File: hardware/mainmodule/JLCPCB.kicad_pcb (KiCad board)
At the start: 2 copper layers, 83.8 x 61 mm, 73 parts, among them J1 USB+, J10 Conn_01x04, J2 To LED_MOD_0, J3 To EXT_MOD_1, J4 V24_IN, J5 Temp, J6 Presence, J7 Neo, J8 AUX, J9 Conn_01x04, Q1 Si3456DDV, Q2 Si3456DDV, Q3 Si3456DDV, Q4 Si3456DDV, Q5 Si3456DDV, Q6 Si3456DDV, SW1 SW_Push, SW2 SW_Push, U1 ESP32-C6-WROOM-1, U3 74HCT244, U4 DS18B20, U5 MC34063AD, U6 DT1042-04SO1

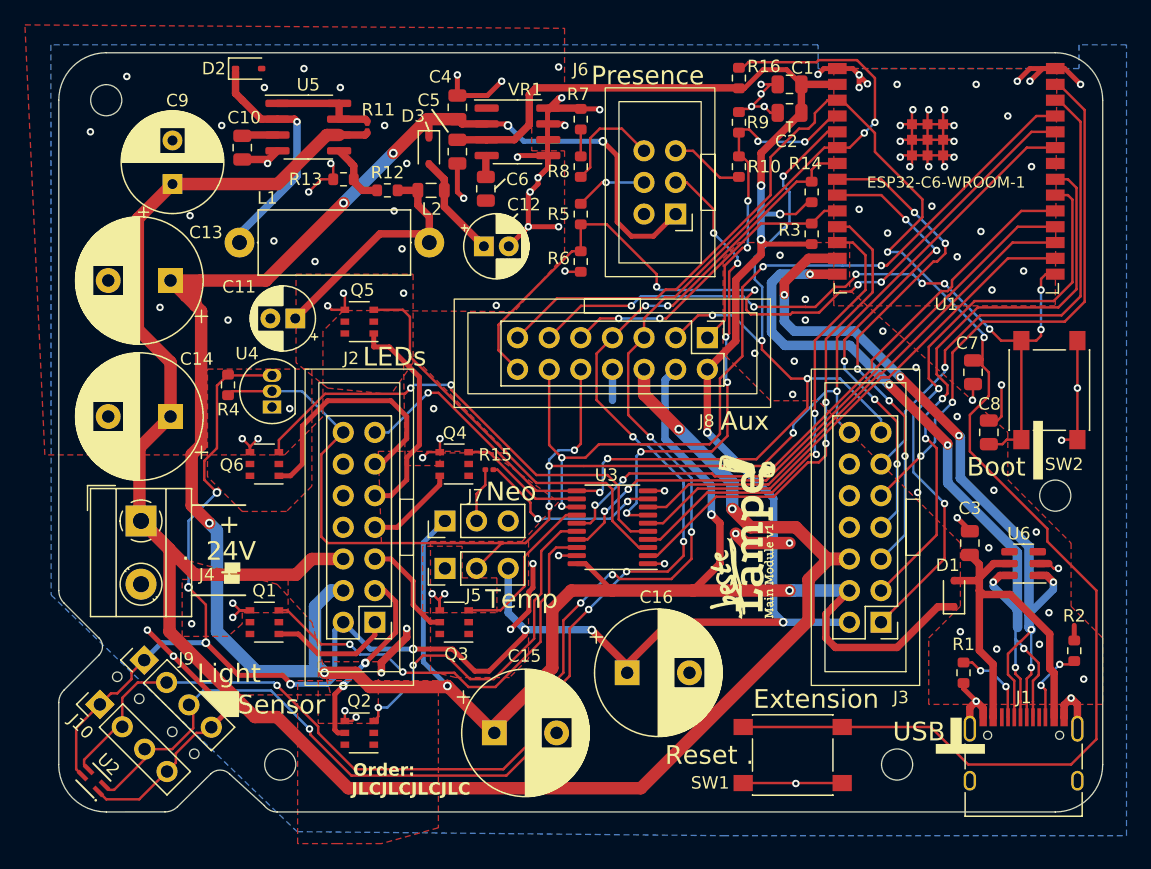
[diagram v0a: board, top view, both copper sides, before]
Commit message: Larger resistor footprints, includes some other property updates.
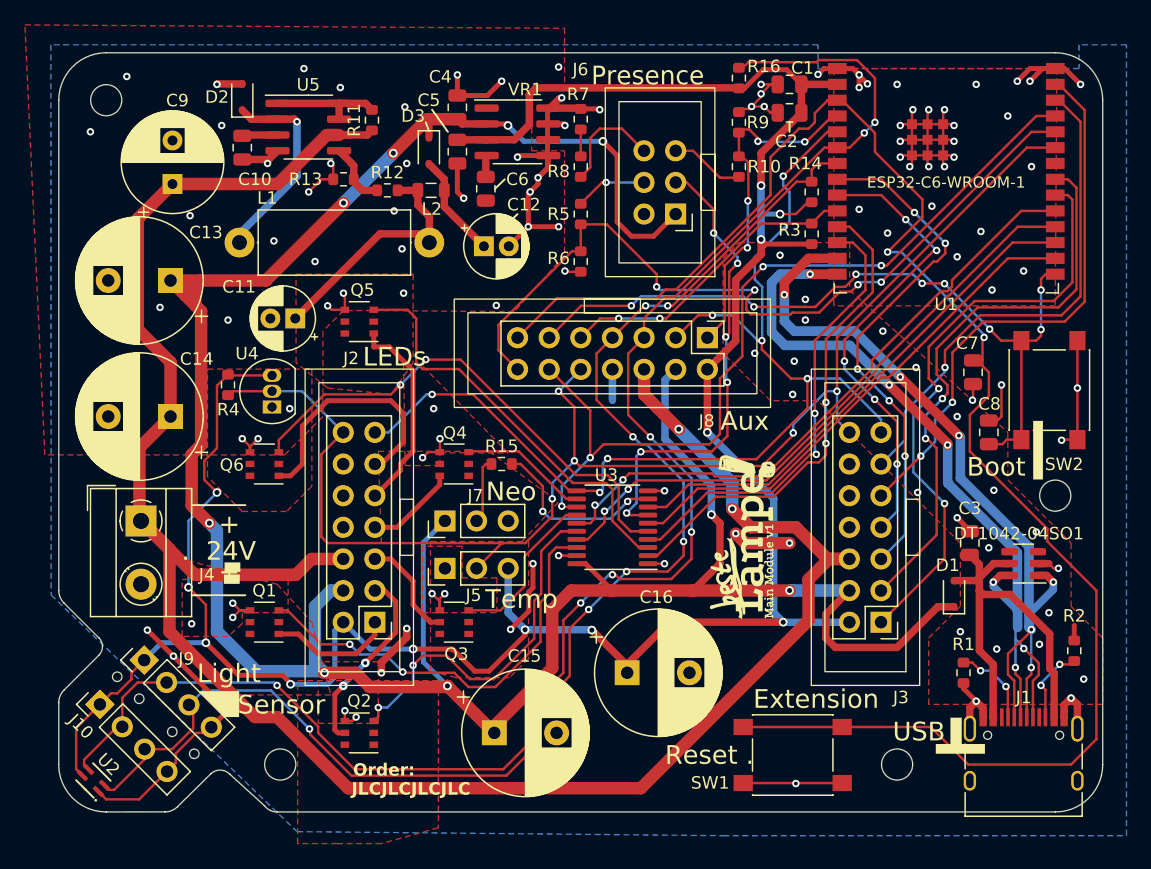
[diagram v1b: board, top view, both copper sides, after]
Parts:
- DT1042-04SO1: renamed from U6; value DT1042-04SO1 -> ~
- R11, R15: footprint Resistor_SMD:R_0201_0603Metric -> Resistor_SMD:R_0603_1608Metric
- U2: renamed from ?; value (none) -> ~
- moved D2 2.34 mm to (79.5, 51.8), turned to 90 degrees
- moved R15 1.09 mm to (100.3, 81.3)
- moved R11 0.68 mm to (89.9, 53.7)
- renumbered H1 to H3
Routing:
- net Net-(D2-K): track 18.8 -> 15.7 mm
- net GND: track 193.4 -> 195.4 mm
- net /TEMP: track 114.8 -> 113.3 mm
- net /DR0.6: track 39.1 -> 40.6 mm
- net /L0.5: track 17.5 -> 16.3 mm
- net Net-(J7-Pin_2): track 4.41 -> 5.33 mm
- net /DR_NEO: track 15.2 -> 14.6 mm
- net Net-(U5-DC): track 8.55 -> 9.07 mm

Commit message: Add two missing EN lines.
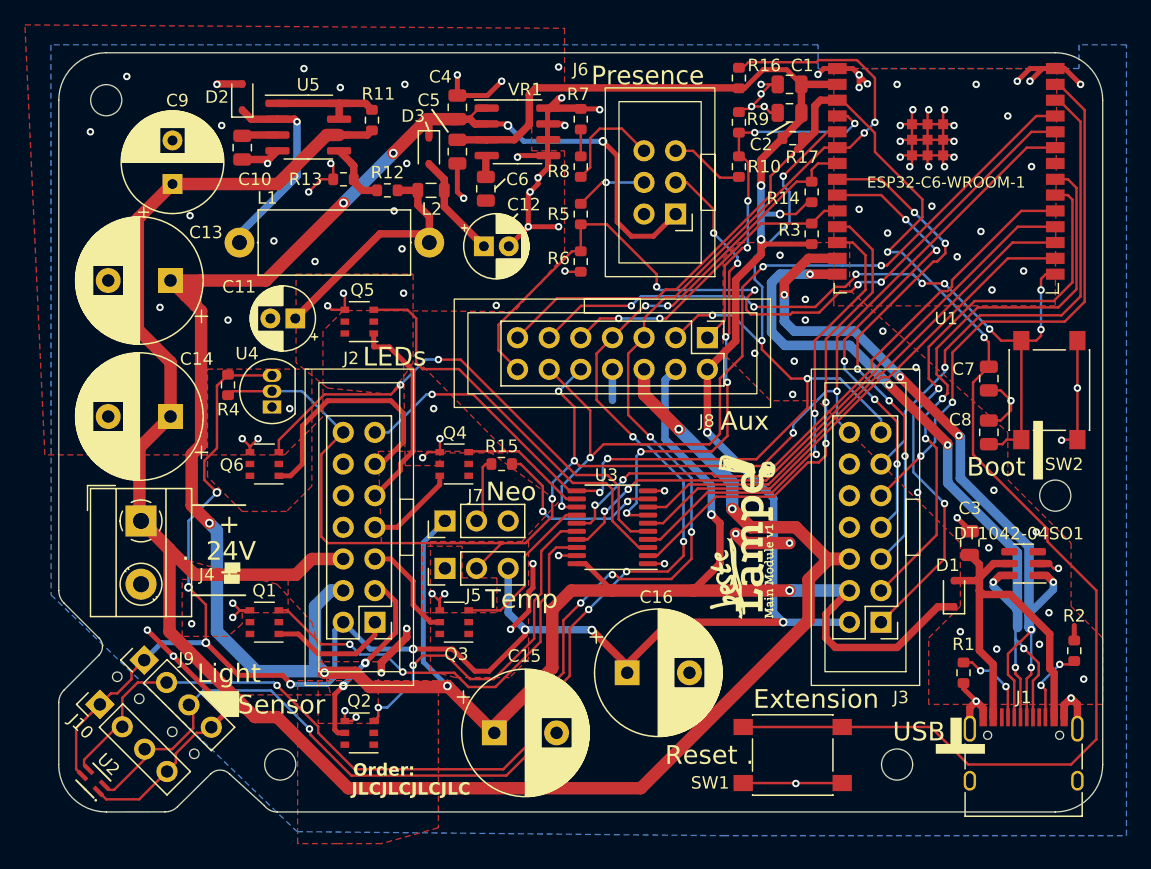
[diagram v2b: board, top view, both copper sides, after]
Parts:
- added R17: 10K, Resistor_SMD:R_0603_1608Metric, F.Cu at (123.7, 55.1)
- moved C7 1.37 mm to (139.4, 74.4)
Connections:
- VR1 pad 1: unconnected-(VR1-EN-Pad1) -> +5V
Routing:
- net +5V: track 215.5 -> 218.6 mm
- net /PRES_A_3V3: track 28.0 -> 30.3 mm
- net GND: vias 120 -> 118

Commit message: Add missing light sensor.
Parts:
- U2: value ~ -> VEML6040A3OG
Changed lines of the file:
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@@
   (footprint "footprints:OPLGA4" (layer "F.Cu")
     (at 67.558883 106.687909 135)
+    (property "LCSC" "C78465")
     (property "Sheetfile" "JLCPCB.kicad_sch")
     (property "Sheetname" "")
@@
         (effects (font (size 0.2 0.2) (thickness 0.05)))
     )
-    (fp_text value "~" (at 0 0.95 135) (layer "F.SilkS") hide
+    (fp_text value "VEML6040A3OG" (at 0 0.95 135) (layer "F.SilkS") hide
         (effects (font (size 0.2 0.2) (thickness 0.05)))
     )

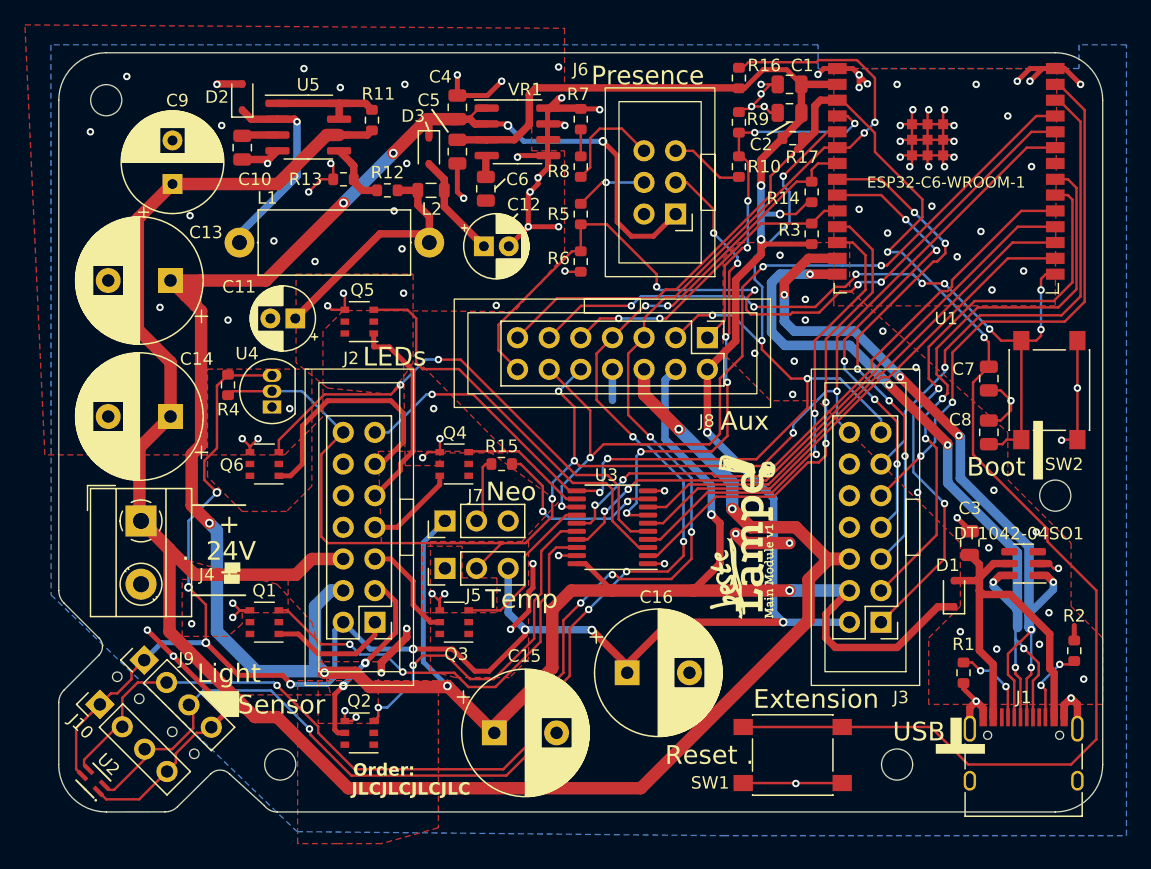
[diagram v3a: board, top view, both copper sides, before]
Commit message: Bigger mounting holes (for M3 screws) and less disconnected ground planes.
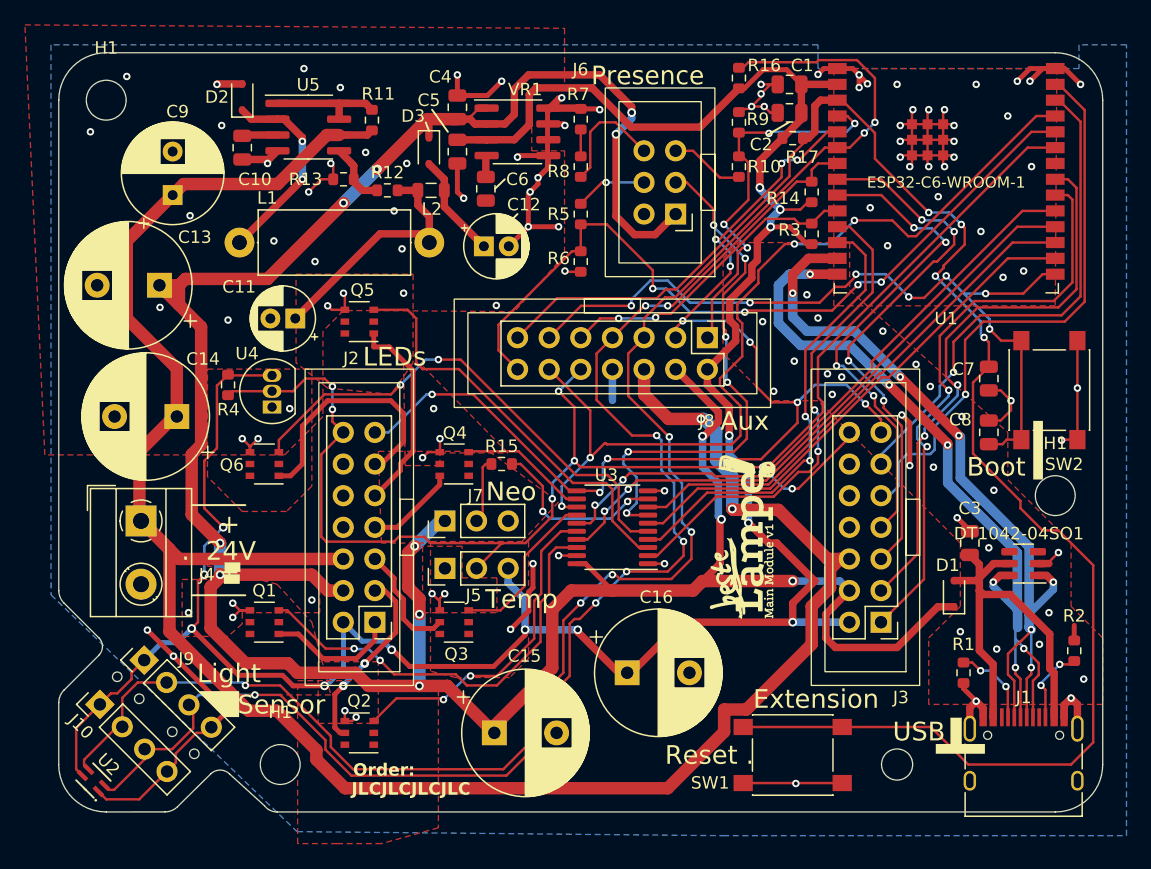
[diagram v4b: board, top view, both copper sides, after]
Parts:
- H1 (x3): footprint MountingHole:MountingHole_2.5mm -> MountingHole:MountingHole_3.2mm_M3
- moved C13 0.97 mm to (72.9, 66.9)
- moved C9 0.89 mm to (73.9, 59.7)
- moved C14 0.51 mm to (74.2, 77.5)
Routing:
- net +5V: track 218.6 -> 229.9 mm, vias 9 -> 12
- net /TEMP: track 113.3 -> 122.4 mm, vias 5 -> 7
- net /PRES_TX_5V: track 38.0 -> 42.6 mm
- net GND: track 195.4 -> 191.0 mm
- net /PRES_TX_3V3: track 69.1 -> 73.0 mm
- net /BOOT9: track 61.5 -> 64.9 mm, vias 8 -> 7
- net /NEO: track 88.6 -> 91.8 mm, vias 7 -> 11
- net /DR0.2: track 29.4 -> 26.7 mm
- net +24V: track 177.8 -> 180.2 mm
- net /L1.4: track 37.5 -> 39.9 mm, vias 5 -> 4
- net /L1.3: track 41.6 -> 43.6 mm, vias 5 -> 4
- net /PRES_RX_3V3: track 65.1 -> 63.3 mm
- net /D+: track 63.6 -> 61.9 mm
- net /PRES_A_3V3: track 30.3 -> 31.9 mm
- net /L1.5: track 44.8 -> 46.3 mm, vias 2 -> 1
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
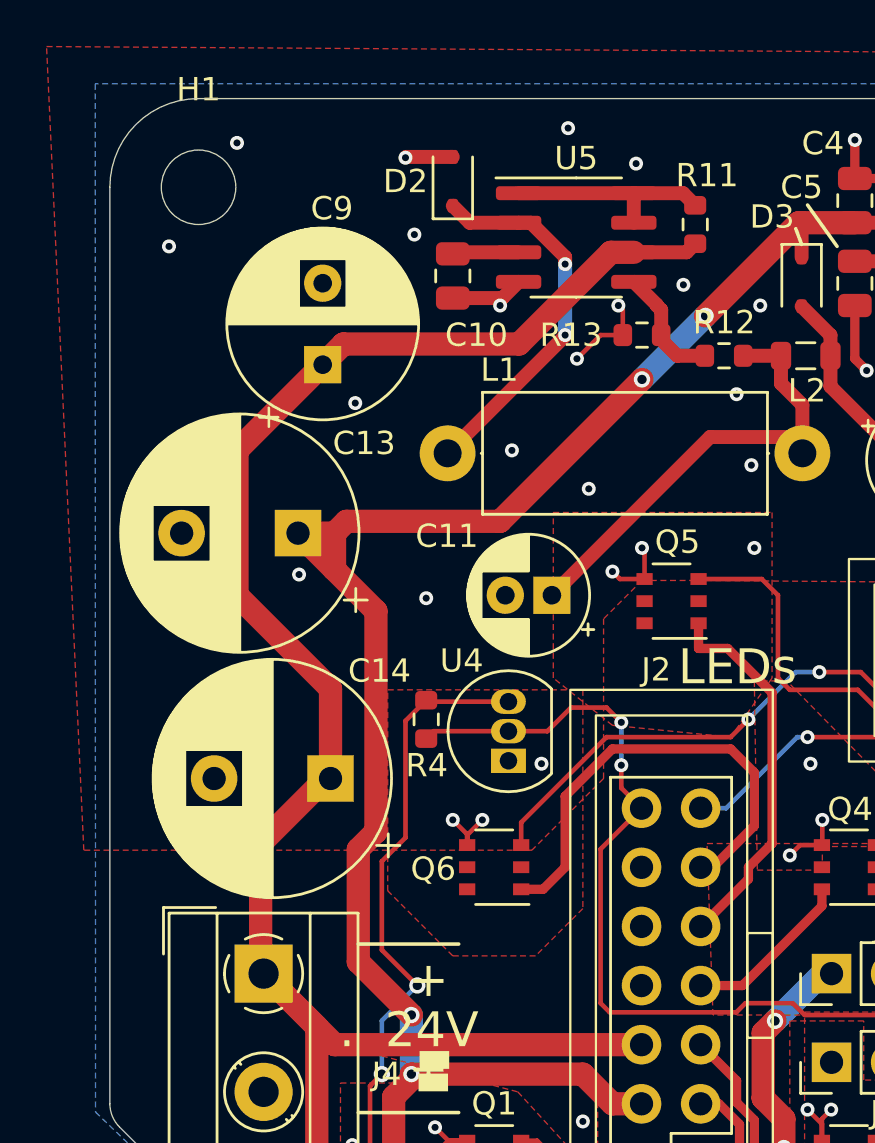
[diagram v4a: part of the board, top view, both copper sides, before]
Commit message: Use SMD version of the temperature sensor.
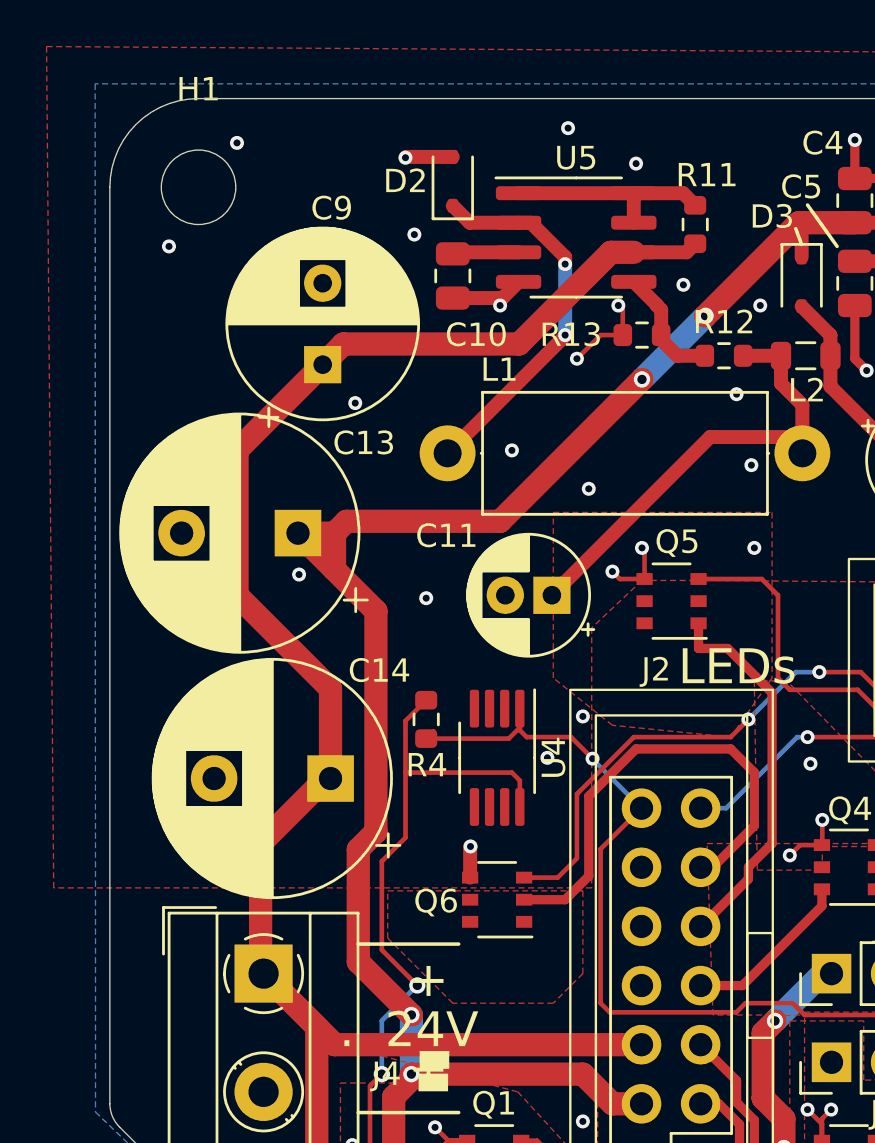
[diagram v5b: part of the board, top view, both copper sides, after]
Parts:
- U4: value DS18B20 -> DS18B20U; footprint Package_TO_SOT_THT:TO-92_Inline -> Package_SO:MSOP-8_3x3mm_P0.65mm
- moved Q6 1.40 mm to (81.4, 82.7)
- moved U4 0.50 mm to (81.4, 76.6), turned to -90 degrees
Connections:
- U4 pad 1: GND -> /TEMP
- U4 pad 2: /TEMP -> unconnected-(U4-NC-Pad2)
- U4 pad 3: +3.3V -> unconnected-(U4-NC-Pad3)
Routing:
- net +3.3V: track 210.8 -> 213.5 mm
- net /DR0.6: track 40.6 -> 42.1 mm
- net GND: track 191.0 -> 189.6 mm
- net /TEMP: track 122.4 -> 122.2 mm, vias 7 -> 6
